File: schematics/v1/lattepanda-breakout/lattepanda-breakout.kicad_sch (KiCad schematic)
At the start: 10 parts, among them J1 RJ45, J2 SDI12, J3 SDI12, J4 Conn_02x04_Odd_Even, J5 Conn_02x15_Odd_Even, J6 Conn_02x02_Odd_Even, U1 MAX22508

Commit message: fix(breakout)
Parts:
- C1: footprint (none) -> Capacitor_SMD:C_0805_2012Metric
- J5: footprint Connector_PinHeader_2.54mm:PinHeader_2x15_P2.54mm_Vertical_SMD -> Connector_PinHeader_2.54mm:PinHeader_2x15_P2.54mm_Vertical
- J6: footprint Connector_PinHeader_2.54mm:PinHeader_2x02_P2.54mm_Vertical_SMD -> Connector_PinHeader_2.54mm:PinHeader_2x02_P2.54mm_Vertical
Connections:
- net +5V: now also J5.27 (Pin_27), J5.29 (Pin_29); no longer J5.30 (Pin_30)
- net GND: now also J5.28 (Pin_28), J5.30 (Pin_30); no longer J5.29 (Pin_29)
- net TX+: now also J3.6; no longer J3.5
- net TX-: now also J3.5; no longer J3.6
- no-connect marks 29 -> 27
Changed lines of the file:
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@@
 	(paper "A4")
+	(junction
+		(at 104.14 81.28)
+		(diameter 0)
+		(color 0 0 0 0)
+	)
 	(junction
 		(at 182.88 38.1)
@@
 		(color 0 0 0 0)
 	)
+	(junction
+		(at 86.36 83.82)
+		(diameter 0)
+		(color 0 0 0 0)
+	)
 	(no_connect
 		(at 88.9 48.26)
@@
 	)
 	(no_connect
-		(at 101.6 81.28)
-	)
-	(no_connect
 		(at 88.9 58.42)
 	)
@@
 	)
 	(no_connect
-		(at 88.9 81.28)
-	)
-	(no_connect
 		(at 88.9 55.88)
 	)
@@
 	(wire
 		(pts
+			(xy 88.9 81.28) (xy 86.36 81.28)
+		)
+		(stroke
+			(width 0)
+			(type default)
+		)
+	)
+	(wire
+		(pts
 			(xy 83.82 35.56) (xy 86.36 35.56)
 		)
@@
 	(wire
 		(pts
+			(xy 88.9 83.82) (xy 86.36 83.82)
+		)
+		(stroke
+			(width 0)
+			(type default)
+		)
+	)
+	(wire
+		(pts
+			(xy 175.26 33.02) (xy 182.88 33.02)
+		)
+		(stroke
+			(width 0)
+			(type default)
+		)
+	)
+	(wire
+		(pts
+			(xy 27.94 38.1) (xy 29.21 38.1)
+		)
+		(stroke
+			(width 0)
+			(type default)
+		)
+	)
+	(wire
+		(pts
+			(xy 46.99 93.98) (xy 45.72 93.98)
+		)
+		(stroke
+			(width 0)
+			(type default)
+		)
+	)
+	(wire
+		(pts
+			(xy 175.26 35.56) (xy 172.72 35.56)
+		)
+		(stroke
+			(width 0)
+			(type default)
+		)
+	)
+	(wire
+		(pts
+			(xy 24.13 68.58) (xy 25.4 68.58)
+		)
+		(stroke
+			(width 0)
+			(type default)
+		)
+	)
+	(wire
+		(pts
+			(xy 139.7 43.18) (xy 139.7 45.72)
+		)
+		(stroke
+			(width 0)
+			(type default)
+		)
+	)
+	(wire
+		(pts
+			(xy 46.99 63.5) (xy 46.99 62.23)
+		)
+		(stroke
+			(width 0)
+			(type default)
+		)
+	)
+	(wire
+		(pts
+			(xy 182.88 33.02) (xy 194.31 33.02)
+		)
+		(stroke
+			(width 0)
+			(type default)
+		)
+	)
+	(wire
+		(pts
+			(xy 27.94 30.48) (xy 29.21 30.48)
+		)
+		(stroke
+			(width 0)
+			(type default)
+		)
+	)
+	(wire
+		(pts
+			(xy 27.94 43.18) (xy 29.21 43.18)
+		)
+		(stroke
+			(width 0)
+			(type default)
+		)
+	)
+	(wire
+		(pts
 			(xy 101.6 83.82) (xy 104.14 83.82)
 		)
@@
 	(wire
 		(pts
-			(xy 175.26 33.02) (xy 182.88 33.02)
-		)
-		(stroke
-			(width 0)
-			(type default)
-		)
-	)
-	(wire
-		(pts
-			(xy 27.94 38.1) (xy 29.21 38.1)
-		)
-		(stroke
-			(width 0)
-			(type default)
-		)
-	)
-	(wire
-		(pts
-			(xy 46.99 93.98) (xy 45.72 93.98)
-		)
-		(stroke
-			(width 0)
-			(type default)
-		)
-	)
-	(wire
-		(pts
-			(xy 175.26 35.56) (xy 172.72 35.56)
-		)
-		(stroke
-			(width 0)
-			(type default)
-		)
-	)
-	(wire
-		(pts
-			(xy 24.13 68.58) (xy 25.4 68.58)
-		)
-		(stroke
-			(width 0)
-			(type default)
-		)
-	)
-	(wire
-		(pts
-			(xy 139.7 43.18) (xy 139.7 45.72)
-		)
-		(stroke
-			(width 0)
-			(type default)
-		)
-	)
-	(wire
-		(pts
-			(xy 46.99 63.5) (xy 46.99 62.23)
-		)
-		(stroke
-			(width 0)
-			(type default)
-		)
-	)
-	(wire
-		(pts
-			(xy 182.88 33.02) (xy 194.31 33.02)
-		)
-		(stroke
-			(width 0)
-			(type default)
-		)
-	)
-	(wire
-		(pts
-			(xy 27.94 30.48) (xy 29.21 30.48)
-		)
-		(stroke
-			(width 0)
-			(type default)
-		)
-	)
-	(wire
-		(pts
-			(xy 27.94 43.18) (xy 29.21 43.18)
-		)
-		(stroke
-			(width 0)
-			(type default)
-		)
-	)
-	(wire
-		(pts
-			(xy 88.9 83.82) (xy 86.36 83.82)
+			(xy 86.36 81.28) (xy 86.36 83.82)
 		)
 		(stroke
@@
 	(wire
 		(pts
+			(xy 101.6 81.28) (xy 104.14 81.28)
+		)
+		(stroke
+			(width 0)
+			(type default)
+		)
+	)
+	(wire
+		(pts
 			(xy 81.28 71.12) (xy 88.9 71.12)
 		)
@@
 	(wire
 		(pts
+			(xy 104.14 78.74) (xy 104.14 81.28)
+		)
+		(stroke
+			(width 0)
+			(type default)
+		)
+	)
+	(wire
+		(pts
 			(xy 182.88 45.72) (xy 194.31 45.72)
 		)
@@
 	(wire
 		(pts
-			(xy 86.36 81.28) (xy 86.36 83.82)
+			(xy 104.14 81.28) (xy 104.14 83.82)
 		)
 		(stroke
@@
 	(wire
 		(pts
-			(xy 104.14 83.82) (xy 104.14 86.36)
+			(xy 86.36 83.82) (xy 86.36 86.36)
 		)
 		(stroke
@@
 		)
 	)
-	(label "TX-"
+	(label "TX+"
 		(at 17.78 93.98 0)
 		(effects
@@
 		)
 	)
-	(label "TX+"
+	(label "TX-"
 		(at 17.78 91.44 0)
 		(effects
@@
 			)
 		)
-		(property "Footprint" "Connector_PinHeader_2.54mm:PinHeader_2x02_P2.54mm_Vertical_SMD"
+		(property "Footprint" "Connector_PinHeader_2.54mm:PinHeader_2x02_P2.54mm_Vertical"
 			(at 93.98 99.06 0)
 			(hide yes)
@@
 			)
 		)
-		(property "Footprint" ""
+		(property "Footprint" "Capacitor_SMD:C_0805_2012Metric"
 			(at 133.6548 34.29 0)
 			(hide yes)
@@
 	(symbol
 		(lib_id "power:GND")
-		(at 104.14 86.36 0)
+		(at 86.36 86.36 0)
+		(mirror y)
 		(unit 1)
 		(body_style 1)
@@
 		(dnp no)
 		(property "Reference" "#PWR02"
-			(at 104.14 92.71 0)
+			(at 86.36 92.71 0)
 			(hide yes)
 			(show_name no)
@@
 		)
 		(property "Value" "GND"
-			(at 104.14 90.678 0)
+			(at 86.36 90.678 0)
 			(show_name no)
 			(do_not_autoplace no)
@@
 		)
 		(property "Footprint" ""
-			(at 104.14 86.36 0)
+			(at 86.36 86.36 0)
 			(hide yes)
 			(show_name no)
@@
 		)
 		(property "Datasheet" ""
-			(at 104.14 86.36 0)
+			(at 86.36 86.36 0)
 			(hide yes)
 			(show_name no)
@@
 		)
 		(property "Description" "Power symbol creates a global label with name \"GND\" , ground"
-			(at 104.14 86.36 0)
+			(at 86.36 86.36 0)
 			(hide yes)
 			(show_name no)
@@
 	(symbol
 		(lib_id "power:+5V")
-		(at 86.36 81.28 0)
+		(at 104.14 78.74 0)
+		(mirror y)
 		(unit 1)
 		(body_style 1)
@@
 		(dnp no)
 		(property "Reference" "#PWR01"
-			(at 86.36 85.09 0)
+			(at 104.14 82.55 0)
 			(hide yes)
 			(show_name no)
@@
 		)
 		(property "Value" "+5V"
-			(at 86.106 77.47 0)
+			(at 104.394 74.93 0)
 			(show_name no)
 			(do_not_autoplace no)
@@
 		)
 		(property "Footprint" ""
-			(at 86.36 81.28 0)
+			(at 104.14 78.74 0)
 			(hide yes)
 			(show_name no)
@@
 		)
 		(property "Datasheet" ""
-			(at 86.36 81.28 0)
+			(at 104.14 78.74 0)
 			(hide yes)
 			(show_name no)
@@
 		)
 		(property "Description" "Power symbol creates a global label with name \"+5V\""
-			(at 86.36 81.28 0)
+			(at 104.14 78.74 0)
 			(hide yes)
 			(show_name no)
@@
 			)
 		)
-		(property "Footprint" "Connector_PinHeader_2.54mm:PinHeader_2x15_P2.54mm_Vertical_SMD"
+		(property "Footprint" "Connector_PinHeader_2.54mm:PinHeader_2x15_P2.54mm_Vertical"
 			(at 96.52 66.04 0)
 			(hide yes)

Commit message: update(lattepanda-breakout)
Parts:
- removed J4: Conn_02x04_Odd_Even, Connector_PinSocket_2.54mm:PinSocket_2x04_P2.54mm_Vertical, symbol Connector_Generic:Conn_02x04_Odd_Even
- removed J5: Conn_02x15_Odd_Even, Connector_PinHeader_2.54mm:PinHeader_2x15_P2.54mm_Vertical, symbol Connector_Generic:Conn_02x15_Odd_Even
- removed J6: Conn_02x02_Odd_Even, Connector_PinHeader_2.54mm:PinHeader_2x02_P2.54mm_Vertical, symbol Connector_Generic:Conn_02x02_Odd_Even
- added C2, C3, C4, C5, C6: 0.1uF, Capacitor_SMD:C_0805_2012Metric, symbol Device:C
- added C7, C8: 1uF, Capacitor_SMD:C_0805_2012Metric, symbol Device:C
- added J1: Arduino, symbol Connector_Generic:Conn_02x05_Odd_Even
- added J2: Arduino, symbol Connector_Generic:Conn_02x06_Odd_Even
- added J3: COM(RS232/485), Connector_PinSocket_2.54mm:PinSocket_2x05_P2.54mm_Vertical, symbol Connector_Generic:Conn_02x05_Odd_Even
- added J4: Front Panel, Connector_PinSocket_2.54mm:PinSocket_2x05_P2.54mm_Vertical, symbol Connector_Generic:Conn_02x05_Odd_Even
- added J7: RS232, Link_Footprints:PC-1053866, symbol Link_Components:PC-1818517
- added J9: RS422, Link_Footprints:PC-1053866, symbol Link_Components:PC-1818517
- added U2: TRSF3232ECD, Link_Footprints:TRFS3232E, symbol Link_Components:TRSF3232ECD
- added U3: TLV75533PDBV, Package_TO_SOT_SMD:SOT-23-5, symbol Regulator_Linear:TLV75533PDBV
- J6: renamed from J3; value SDI12 -> RS485
- J8: renamed from J1; value RJ45 -> PiKVM
- renumbered J2 to J5, R2 to R1, R1 to R2
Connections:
- net +5V: now also C7.1, J2.11 (Pin_11), J2.9 (Pin_9), J7.4, J9.4, U3.1 (IN), U3.3 (EN)
- net BTN_PWR_{+}: now also J4.7 (Pin_7)
- net BTN_PWR_{-}: now also J4.5 (Pin_5)
- net BTN_RST_{+}: now also J4.6 (Pin_6)
- net BTN_RST_{-}: now also J4.8 (Pin_8)
- net GND: now also C4.1, C5.2, C6.2, C7.2, C8.2, J2.10 (Pin_10), J2.12 (Pin_12), J3.6 (Pin_6), J7.3, J9.3, U2.15 (GND), U3.2 (GND)
- net LED_HDD_{+}: now also J4.2 (Pin_2)
- net LED_HDD_{-}: now also J4.4 (Pin_4)
- net LED_PWR_{+}: now also J4.1 (Pin_1)
- net LED_PWR_{-}: now also J4.3 (Pin_3)
- net RX: now also J1.7 (Pin_7)
- net SDI12: now also J2.2 (Pin_2)
- net TX: now also J1.9 (Pin_9)
- new net: C4.2, U2.6 (V-)
- new net: C2.1, U2.1 (C1+)
- new net: C5.1, U2.2 (V+)
- new net: C2.2, U2.3 (C1-)
- new net: C3.1, U2.4 (C2+)
- new net: C3.2, U2.5 (C2-)
- new net +3V3: C6.1, C8.1, U2.16 (VCC), U3.5 (OUT)
- new net 422_RX+: J9.1
- new net 422_RX-: J9.2
- new net 422_TX+: J9.5
- new net 422_TX-: J9.6
- new net CTS: J3.3 (Pin_3)
- new net DSR: J3.5 (Pin_5)
- new net DTR: J3.7 (Pin_7)
- new net GPS_PPS: J7.6, U2.10 (DIN2)
- new net GPS_RX: J7.2, U2.13 (RIN1)
- new net GPS_TX: J7.5, U2.11 (DIN1)
- new net LP_DCD: J3.10 (Pin_10), U2.7 (DOUT2)
- new net LP_RX: J3.9 (Pin_9), U2.14 (DOUT1)
- new net LP_TX: J3.8 (Pin_8), U2.12 (ROUT1)
- new net RI: J3.2 (Pin_2)
- new net RTS: J3.4 (Pin_4)
- no-connect marks 27 -> 34
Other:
- note added: "External Connectors"
- note added: "LattePanda Connectors"
- moved on the sheet: C1, J5, J6, J8, R1, R2, U1

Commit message: update(lattepanda-breakout): still need to To make routing a little bit easier, could switch to 4 layer 1. Finish routing for RS232 2. Add differentials for RS422 to tsd 3. Consider switching connectors? 4. Verify wiring of Rj45 connector (changed from original breakout)
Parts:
- C1, C2, C3, C4, C5, C6, C7, C8: footprint Capacitor_SMD:C_0805_2012Metric -> Capacitor_SMD:C_0603_1608Metric
- J1: footprint (none) -> Connector_PinHeader_2.54mm:PinHeader_2x05_P2.54mm_Vertical
- J2: footprint (none) -> Connector_PinHeader_2.54mm:PinHeader_2x06_P2.54mm_Vertical_SMD
- J8: footprint Connector_RJ:RJ45_Amphenol_54602-x08_Horizontal -> Link_Footprints:rj45_smd
- R1, R2: footprint Resistor_SMD:R_0805_2012Metric -> Resistor_SMD:R_0603_1608Metric
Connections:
- net 422_RX+ renamed 422_PPS+
- net 422_RX- renamed 422_PPS-
- net RX renamed 485_RX
- net RX+ renamed 485_RX+
- net 485_RX+: now also J6.6; no longer J6.1
- net RX- renamed 485_RX-
- net 485_RX-: now also J6.5; no longer J6.2
- net TX renamed 485_TX
- net TX+ renamed 485_TX+
- net 485_TX+: now also J6.1; no longer J6.6
- net TX- renamed 485_TX-
- net 485_TX-: now also J6.2; no longer J6.5
- no-connect marks 34 -> 26
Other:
- moved on the sheet: C1, J6, R1, R2, U1

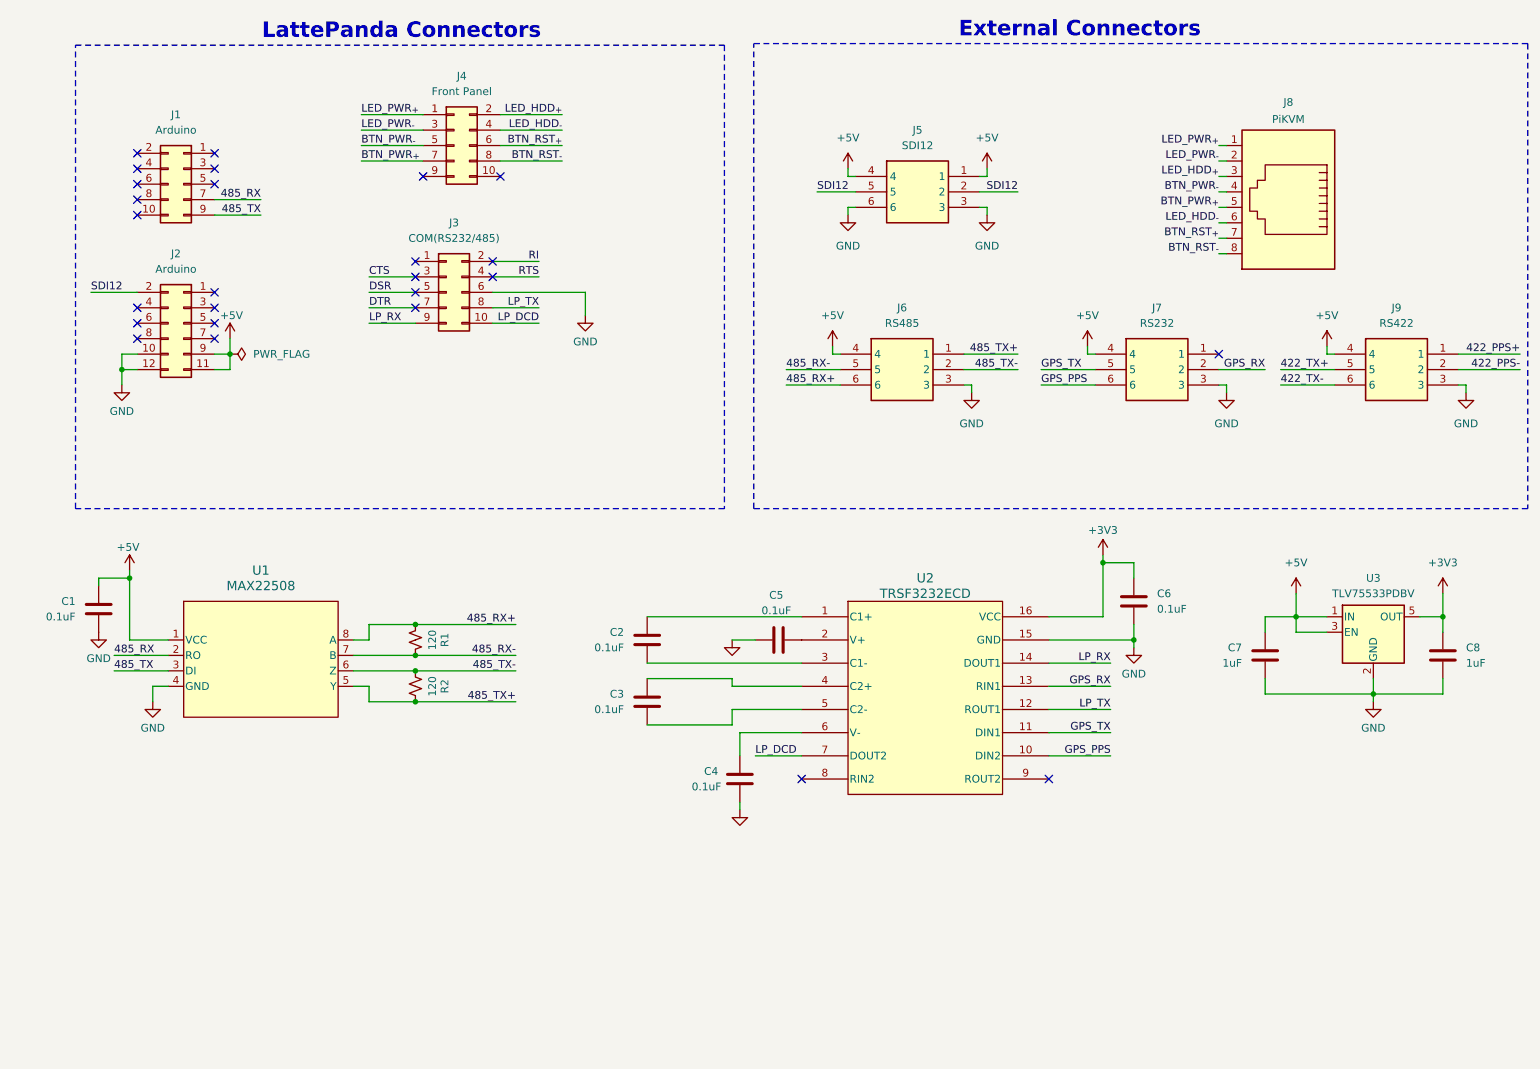
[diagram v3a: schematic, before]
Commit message: Add rs422 GPS breakout to LP breakout
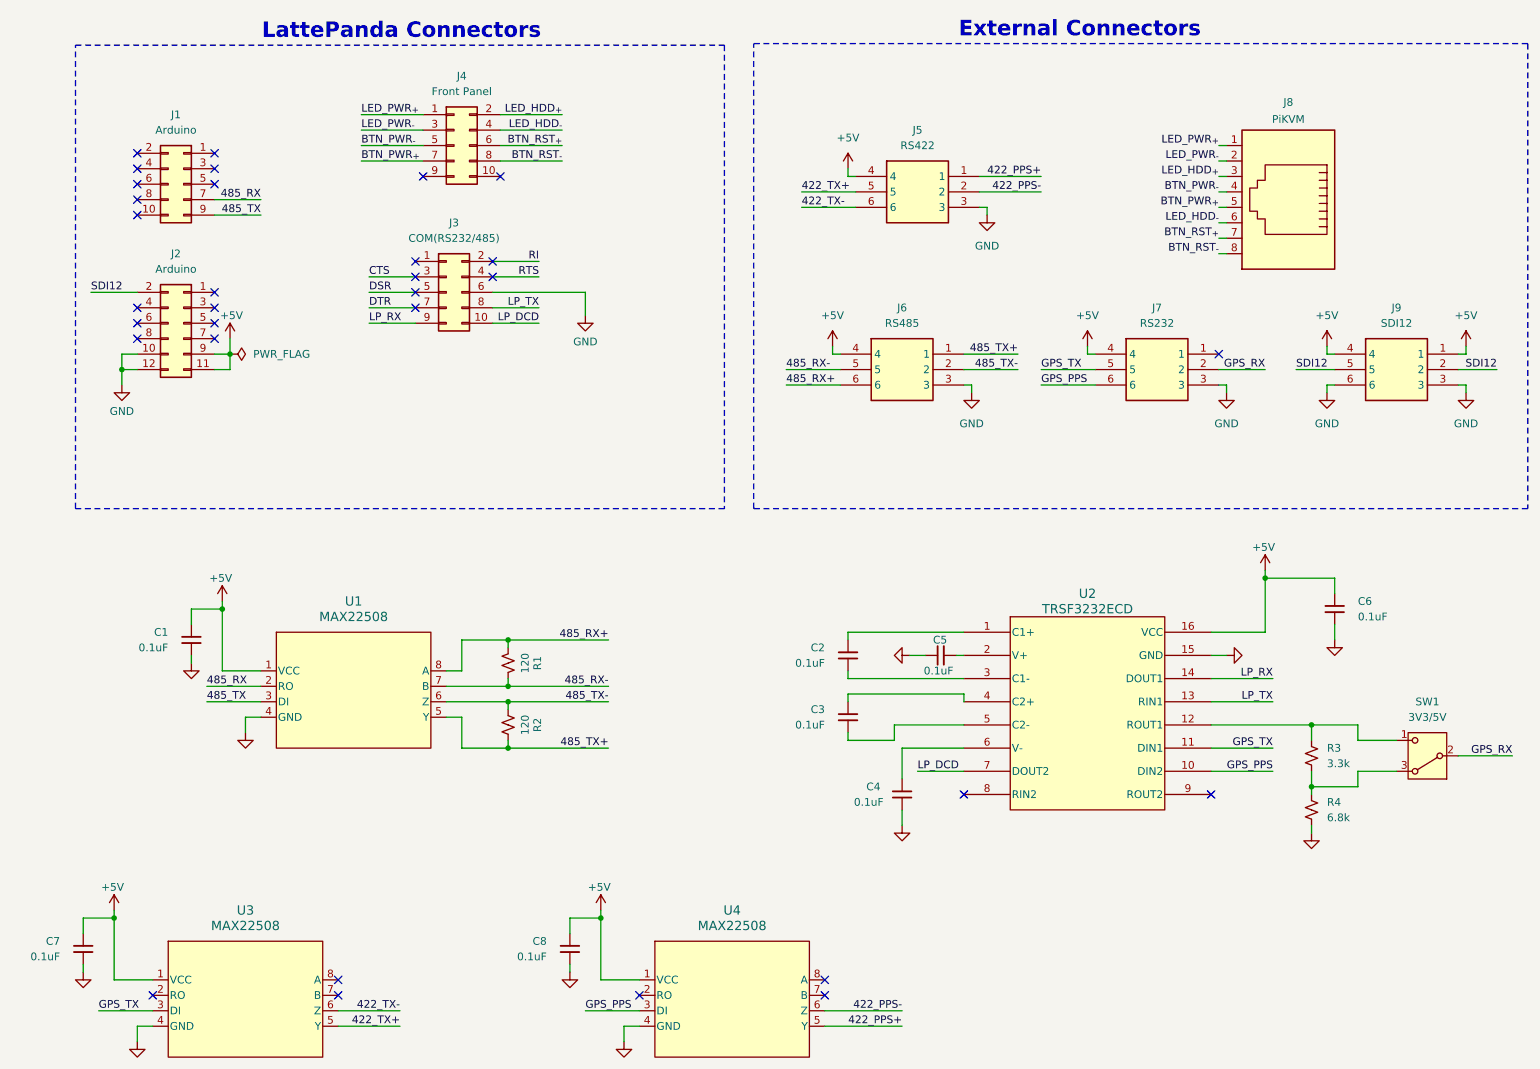
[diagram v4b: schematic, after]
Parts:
- removed C7, C8: 1uF, Capacitor_SMD:C_0603_1608Metric, symbol Device:C
- removed U3: TLV75533PDBV, Package_TO_SOT_SMD:SOT-23-5, symbol Regulator_Linear:TLV75533PDBV
- added C7, C8: 0.1uF, Capacitor_SMD:C_0603_1608Metric, symbol Device:C_Small
- added R3: 3.3k, Resistor_SMD:R_0603_1608Metric, symbol Device:R_Small_US
- added R4: 6.8k, Resistor_SMD:R_0603_1608Metric, symbol Device:R_Small_US
- added SW1: 3V3/5V, Button_Switch_SMD:Nidec_Copal_CAS-120A, symbol Switch:SW_Nidec_CAS-120A1
- added U3, U4: MAX22508, Link_Footprints:MAX22508, symbol Link_Components:MAX22508
- C1, C2, C3, C4, C5, C6: symbol Device:C -> Device:C_Small
- J5: value SDI12 -> RS422
- J9: value RS422 -> SDI12
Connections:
- net +3V3 is gone; now on net +5V: C6.1, U2.16 (VCC)
- net +5V: now also J9.1, C7.1, C8.1, U3.1 (VCC), U4.1 (VCC); no longer J5.1
- net 422_PPS+: now also J5.1, U4.5 (Y); no longer J9.1
- net 422_PPS-: now also J5.2, U4.6 (Z); no longer J9.2
- net 422_TX+: now also J5.5, U3.5 (Y); no longer J9.5
- net 422_TX-: now also J5.6, U3.6 (Z); no longer J9.6
- net GND: now also J9.6, C7.2, C8.2, R4.2, U3.4 (GND), U4.4 (GND); no longer J5.6
- net GPS_PPS: now also U4.3 (DI)
- net GPS_RX: now also SW1.2 (B); no longer U2.13 (RIN1)
- net GPS_TX: now also U3.3 (DI)
- net LP_TX: now also U2.13 (RIN1); no longer U2.12 (ROUT1)
- net SDI12: now also J9.2, J9.5; no longer J5.2, J5.5
- new net: R3.2, R4.1, SW1.3 (A)
- new net: R3.1, SW1.1 (C), U2.12 (ROUT1)
- no-connect marks 26 -> 32
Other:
- moved on the sheet: C1, C2, C3, C4, C5, C6, R1, R2, U1, U2

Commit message: lattepanda-breakout finish
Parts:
- C1, C2, C3, C4, C5, C6, C7, C8: MPN (none) -> C0603C104K5RACTU
- J1: MPN (none) -> 10129381-910004BLF
- J2: MPN (none) -> 10129381-912004BLF
- J3, J4: MPN (none) -> SSK04-FPH-254-B5
- J5: footprint Link_Footprints:PC-1053866 -> 1818517; MPN (none) -> 1818517; Manufacturer_Name Phoenix Contact -> (none); Manufacturer_Part_Number 1818517 -> (none); Mouser Part Number 651-1818517 -> (none); Mouser Price/Stock https://www.mouser.co.uk/ProductDetail/Phoenix-Contact/1818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 -> (none)
- J6, J7, J9: footprint Link_Footprints:PC-1053866 -> 1818517; MPN (none) -> 1818517; Manufacturer_Part_Number 1818517 -> (none); Mouser Part Number 651-1818517 -> (none); Mouser Price/Stock https://www.mouser.co.uk/ProductDetail/Phoenix-Contact/1818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 -> (none)
- J8: MPN (none) -> 1433900000
- R1, R2: MPN (none) -> RMEF0603JT120R
- R3: MPN (none) -> RMEF0603JT3K30
- R4: MPN (none) -> CRG0603F6K8
- SW1: symbol Switch:SW_Nidec_CAS-120A1 -> Link_Components:SW_Nidec_CAS-120A1; MPN (none) -> CAS-120TA
- U1, U3, U4: footprint Link_Footprints:MAX22508 -> 21-0041_S8+2C_MXM; MPN (none) -> MAX22508EASA+
- U2: footprint Link_Footprints:TRFS3232E -> D16; MPN (none) -> TRSF3232ECDR
